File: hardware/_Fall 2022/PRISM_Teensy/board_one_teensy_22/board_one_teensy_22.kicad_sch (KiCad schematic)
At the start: 15 parts, among them J1 EAST, J2 CORE_IO, J3 USB_micro, U1 Teensy4.1, U2 BNO055_Breakout, U3 3966

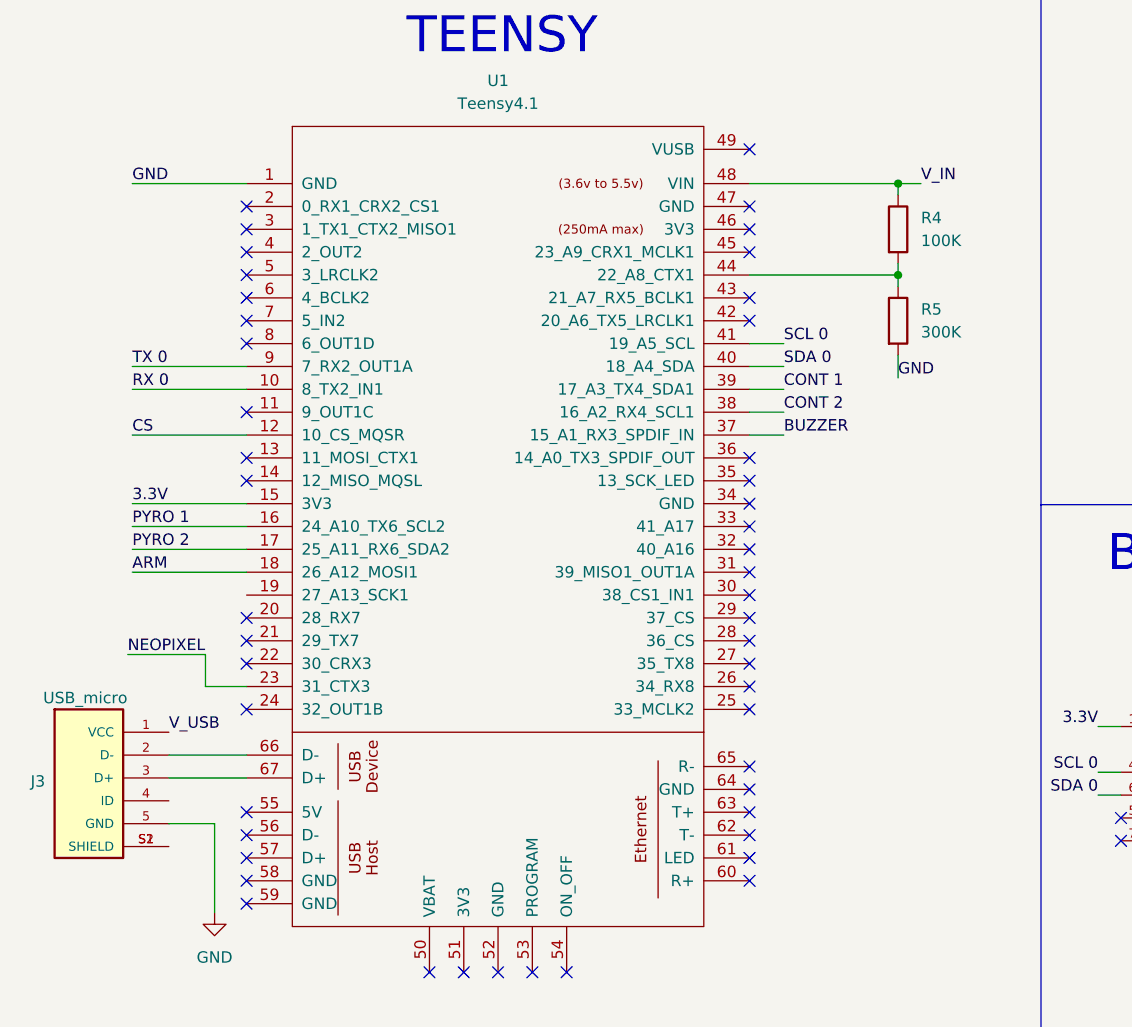
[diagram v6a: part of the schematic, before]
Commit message: Edit footprint layout and resistor sizes
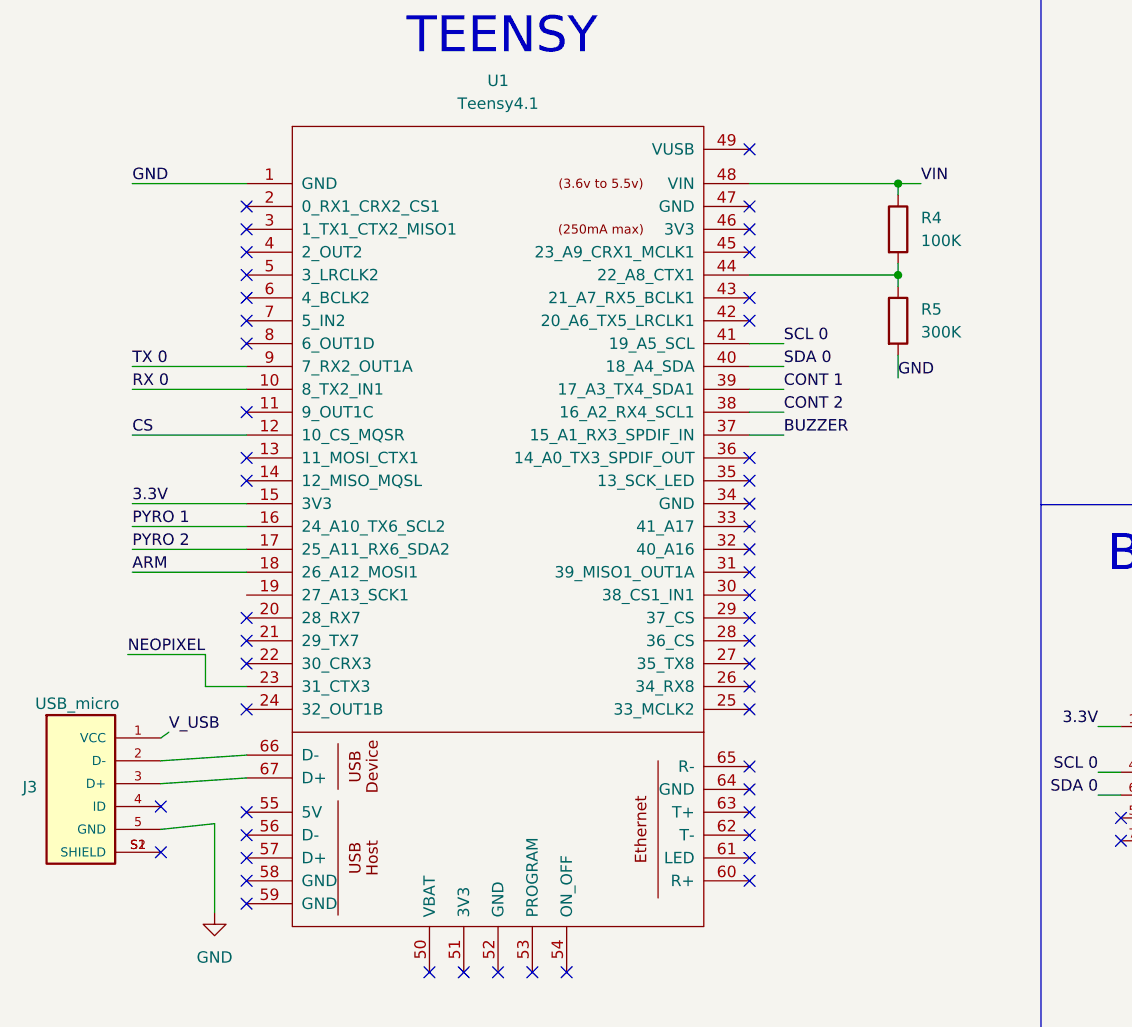
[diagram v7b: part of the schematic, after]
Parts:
- C1: footprint Capacitor_SMD:C_0805_2012Metric_Pad1.18x1.45mm_HandSolder -> Capacitor_SMD:C_0201_0603Metric
- C2: footprint Capacitor_Tantalum_SMD:CP_EIA-1608-08_AVX-J -> Capacitor_SMD:C_0201_0603Metric
- R4, R5: footprint Resistor_SMD:R_0805_2012Metric_Pad1.20x1.40mm_HandSolder -> Resistor_SMD:R_0201_0603Metric
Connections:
- net V_IN is gone; now on net VIN: R4.1, U1.48 (VIN)
- no-connect marks 58 -> 60
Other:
- moved on the sheet: J3
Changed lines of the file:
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@@
   )
   (no_connect (at 163.068 44.958))
+  (no_connect (at 27.94 104.14))
+  (no_connect (at 27.94 109.22))
   (no_connect (at 93.345 42.545))
   (no_connect (at 93.345 40.005))
@@
     (stroke (width 0) (type default) (color 0 0 0 0))
   )
-  (wire (pts (xy 28.829 98.425) (xy 37.465 98.425))
+  (wire (pts (xy 27.94 99.06) (xy 37.465 98.425))
     (stroke (width 0) (type default) (color 0 0 0 0))
   )
@@
     (stroke (width 0) (type default) (color 0 0 0 0))
   )
-  (wire (pts (xy 28.829 100.965) (xy 37.465 100.965))
+  (wire (pts (xy 27.94 101.6) (xy 37.465 100.965))
     (stroke (width 0) (type default) (color 0 0 0 0))
   )
@@
     (stroke (width 0) (type default) (color 0 0 0 0))
   )
-  (wire (pts (xy 33.909 106.045) (xy 28.829 106.045))
+  (wire (pts (xy 33.909 106.045) (xy 27.94 106.68))
     (stroke (width 0) (type default) (color 0 0 0 0))
   )
@@
   )
   (wire (pts (xy 208.788 35.306) (xy 198.628 35.306))
+    (stroke (width 0) (type default) (color 0 0 0 0))
+  )
+  (wire (pts (xy 27.94 96.52) (xy 28.829 95.885))
     (stroke (width 0) (type default) (color 0 0 0 0))
   )
@@
     (effects (font (size 1.27 1.27)) (justify left bottom))
   )
-  (label "V_IN" (at 112.395 34.925 0)
+  (label "VIN" (at 112.395 34.925 0)
     (effects (font (size 1.27 1.27)) (justify left bottom))
   )
@@
       (effects (font (size 1.27 1.27)) (justify left))
     )
-    (property "Footprint" "Capacitor_Tantalum_SMD:CP_EIA-1608-08_AVX-J" (id 2) (at 242.6208 38.354 0)
+    (property "Footprint" "Capacitor_SMD:C_0201_0603Metric" (id 2) (at 242.6208 38.354 0)
       (effects (font (size 1.27 1.27)) hide)
     )
@@
       (effects (font (size 1.27 1.27)) (justify left))
     )
-    (property "Footprint" "Resistor_SMD:R_0805_2012Metric_Pad1.20x1.40mm_HandSolder" (id 2) (at 108.077 40.005 90)
+    (property "Footprint" "Resistor_SMD:R_0201_0603Metric" (id 2) (at 108.077 40.005 90)
       (effects (font (size 1.27 1.27)) hide)
     )
@@
       (effects (font (size 1.27 1.27)) (justify left))
     )
-    (property "Footprint" "Resistor_SMD:R_0805_2012Metric_Pad1.20x1.40mm_HandSolder" (id 2) (at 108.077 50.165 90)
+    (property "Footprint" "Resistor_SMD:R_0201_0603Metric" (id 2) (at 108.077 50.165 90)
       (effects (font (size 1.27 1.27)) hide)
     )
@@
     (pin "2")
   )
-  (symbol (lib_id "USB:USB3131-30-0230-A_REVB") (at 19.939 102.235 0) (unit 1)
+  (symbol (lib_id "USB:USB3131-30-0230-A_REVB") (at 19.05 102.87 0) (unit 1)
     (in_bom yes) (on_board yes)
-    (property "Reference" "J3" (id 0) (at 13.462 101.346 0)
-      (effects (font (size 1.27 1.27)) (justify left))
-    )
-    (property "Value" "USB_micro" (id 1) (at 14.859 92.075 0)
-      (effects (font (size 1.27 1.27)) (justify left))
-    )
-    (property "Footprint" "USB:GCT_USB3131-30-0230-A_REVB" (id 2) (at 23.749 113.665 0)
+    (property "Reference" "J3" (id 0) (at 12.573 101.981 0)
+      (effects (font (size 1.27 1.27)) (justify left))
+    )
+    (property "Value" "USB_micro" (id 1) (at 13.97 92.71 0)
+      (effects (font (size 1.27 1.27)) (justify left))
+    )
+    (property "Footprint" "USB:GCT_USB3131-30-0230-A_REVB" (id 2) (at 22.86 114.3 0)
       (effects (font (size 1.27 1.27)) (justify bottom) hide)
     )
-    (property "Datasheet" "" (id 3) (at 21.209 103.505 0)
-      (effects (font (size 1.27 1.27)) hide)
-    )
-    (property "PARTREV" "" (id 4) (at 21.209 103.505 0)
+    (property "Datasheet" "" (id 3) (at 20.32 104.14 0)
+      (effects (font (size 1.27 1.27)) hide)
+    )
+    (property "PARTREV" "" (id 4) (at 20.32 104.14 0)
       (effects (font (size 1.27 1.27)) (justify bottom) hide)
     )
-    (property "MANUFACTURER" "" (id 5) (at 21.209 103.505 0)
+    (property "MANUFACTURER" "" (id 5) (at 20.32 104.14 0)
       (effects (font (size 1.27 1.27)) (justify bottom) hide)
     )
-    (property "STANDARD" "" (id 6) (at 21.209 103.505 0)
+    (property "STANDARD" "" (id 6) (at 20.32 104.14 0)
       (effects (font (size 1.27 1.27)) (justify bottom) hide)
     )
-    (property "MAXIMUM_PACKAGE_HEIGHT" "" (id 7) (at 21.209 103.505 0)
+    (property "MAXIMUM_PACKAGE_HEIGHT" "" (id 7) (at 20.32 104.14 0)
       (effects (font (size 1.27 1.27)) (justify bottom) hide)
     )
@@
       (effects (font (size 1.27 1.27)) (justify left))
     )
-    (property "Footprint" "Capacitor_SMD:C_0805_2012Metric_Pad1.18x1.45mm_HandSolder" (id 2) (at 255.8542 93.98 0)
+    (property "Footprint" "Capacitor_SMD:C_0201_0603Metric" (id 2) (at 255.8542 93.98 0)
       (effects (font (size 1.27 1.27)) hide)
     )
@@
     )
     (path "/ed2d98ad-ef42-4a14-aff6-3752d42a2ad5"
-      (reference "C1") (unit 1) (value "0.1uf") (footprint "Capacitor_SMD:C_0805_2012Metric_Pad1.18x1.45mm_HandSolder")
+      (reference "C1") (unit 1) (value "0.1uf") (footprint "Capacitor_SMD:C_0201_0603Metric")
     )
     (path "/8ed0ca95-1fef-48eb-87fb-7d2d377cf6d8"
-      (reference "C2") (unit 1) (value "0.1uf") (footprint "Capacitor_Tantalum_SMD:CP_EIA-1608-08_AVX-J")
+      (reference "C2") (unit 1) (value "0.1uf") (footprint "Capacitor_SMD:C_0201_0603Metric")
     )
     (path "/fed88b2e-3769-4111-82b6-285fe17003ad"
@@
     )
     (path "/99baa0dd-fde4-4b75-83f6-a1af8f8c4b2c"
-      (reference "R4") (unit 1) (value "100K") (footprint "Resistor_SMD:R_0805_2012Metric_Pad1.20x1.40mm_HandSolder")
+      (reference "R4") (unit 1) (value "100K") (footprint "Resistor_SMD:R_0201_0603Metric")
     )
     (path "/b35b9880-c31b-4cfc-ab23-116f0c0cec40"
-      (reference "R5") (unit 1) (value "300K") (footprint "Resistor_SMD:R_0805_2012Metric_Pad1.20x1.40mm_HandSolder")
+      (reference "R5") (unit 1) (value "300K") (footprint "Resistor_SMD:R_0201_0603Metric")
     )
     (path "/fefe5b14-c21f-486c-b97d-175c68b72866"
